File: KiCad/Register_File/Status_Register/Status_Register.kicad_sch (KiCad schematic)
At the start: 43 parts, among them J1 Conn_01x02_Pin, J10 Conn_01x02_Pin, J11 Conn_01x04_Pin, J2 Conn_01x02_Pin, J3 Conn_01x02_Pin, J5 Conn_01x08_Pin, J6 Conn_01x04_Pin, J7 Conn_01x04_Pin, SW2 SW_SPDT, U1 74LS173, U2 74LS173, U3 74LS245, U4 74LS157, U5 74LS157, U6 74LS08, U7 74LS04, U8 74LS245

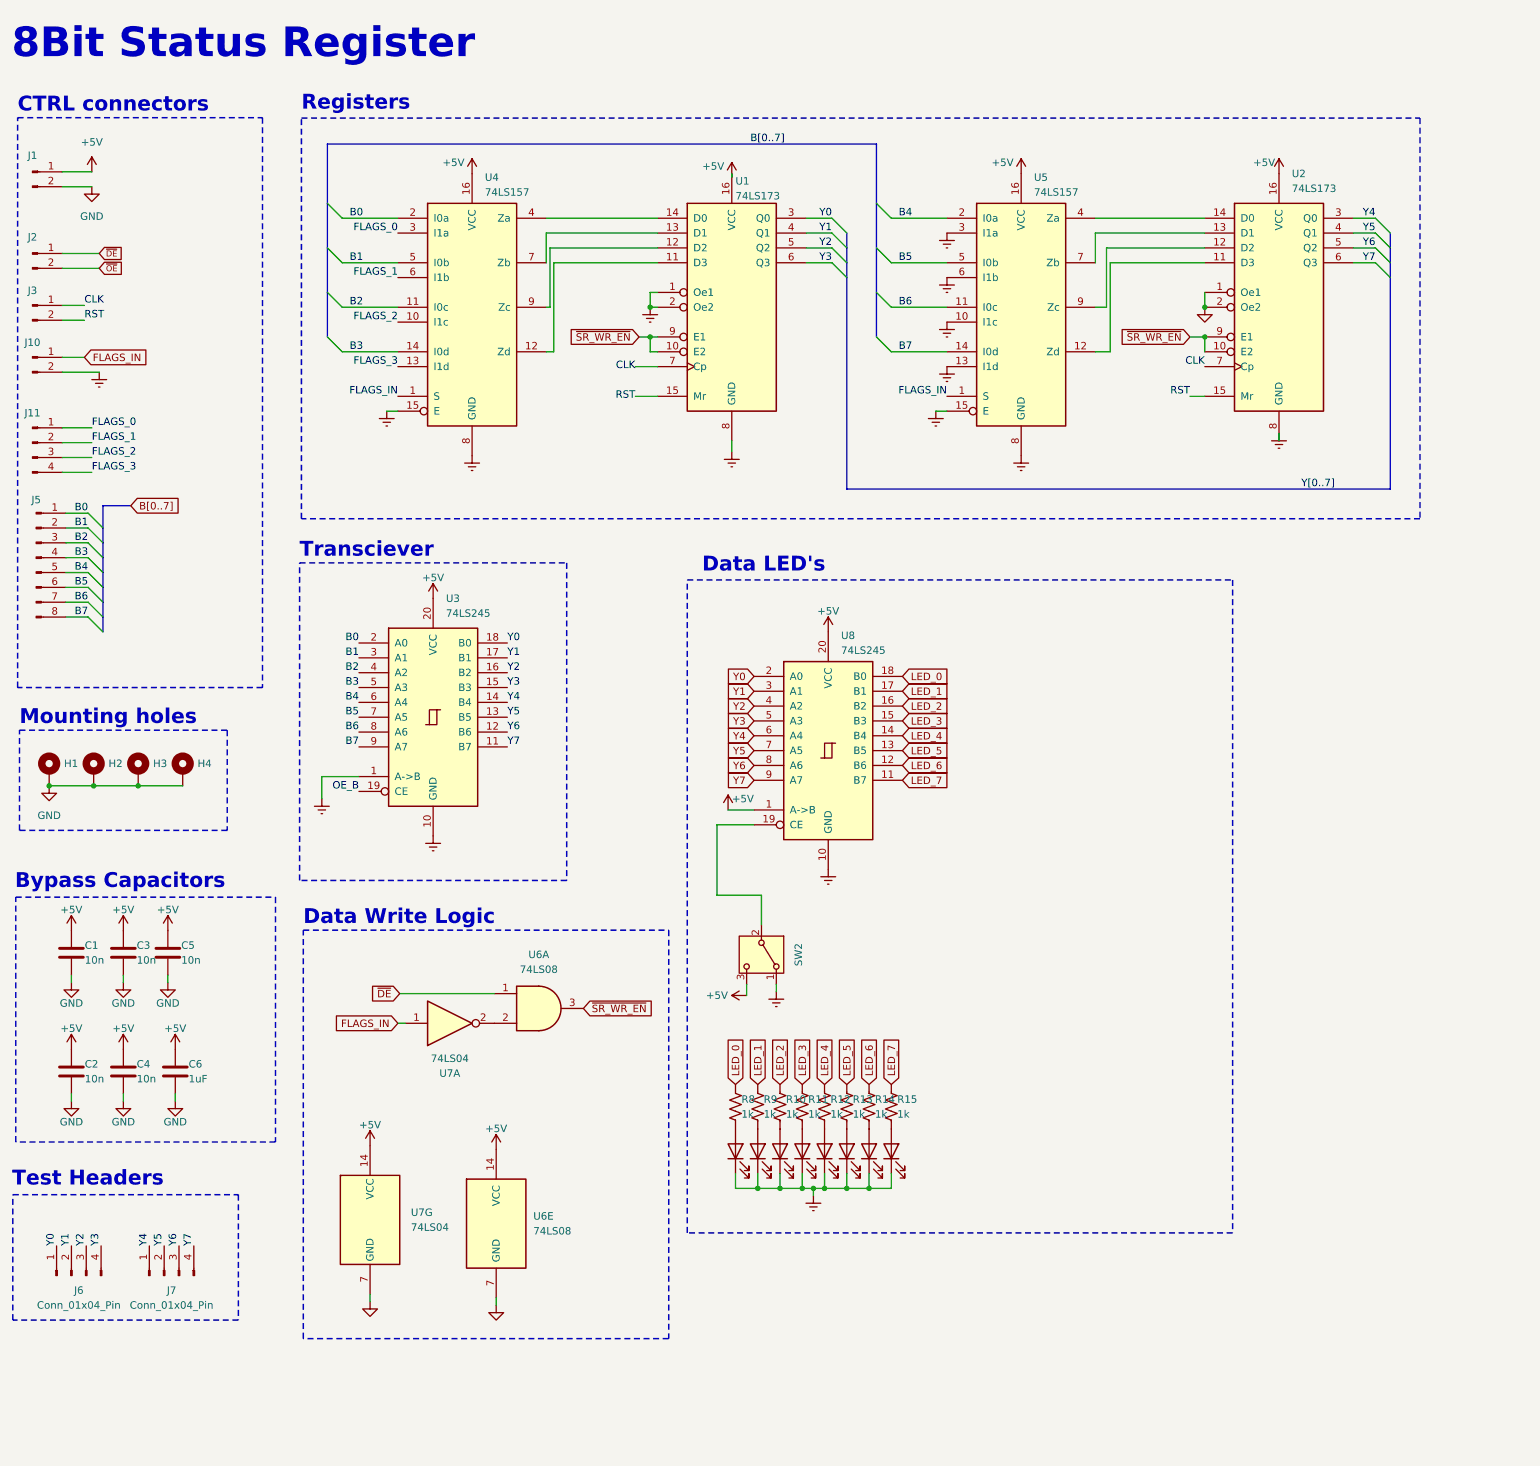
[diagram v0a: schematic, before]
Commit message: created standarts for PCB's
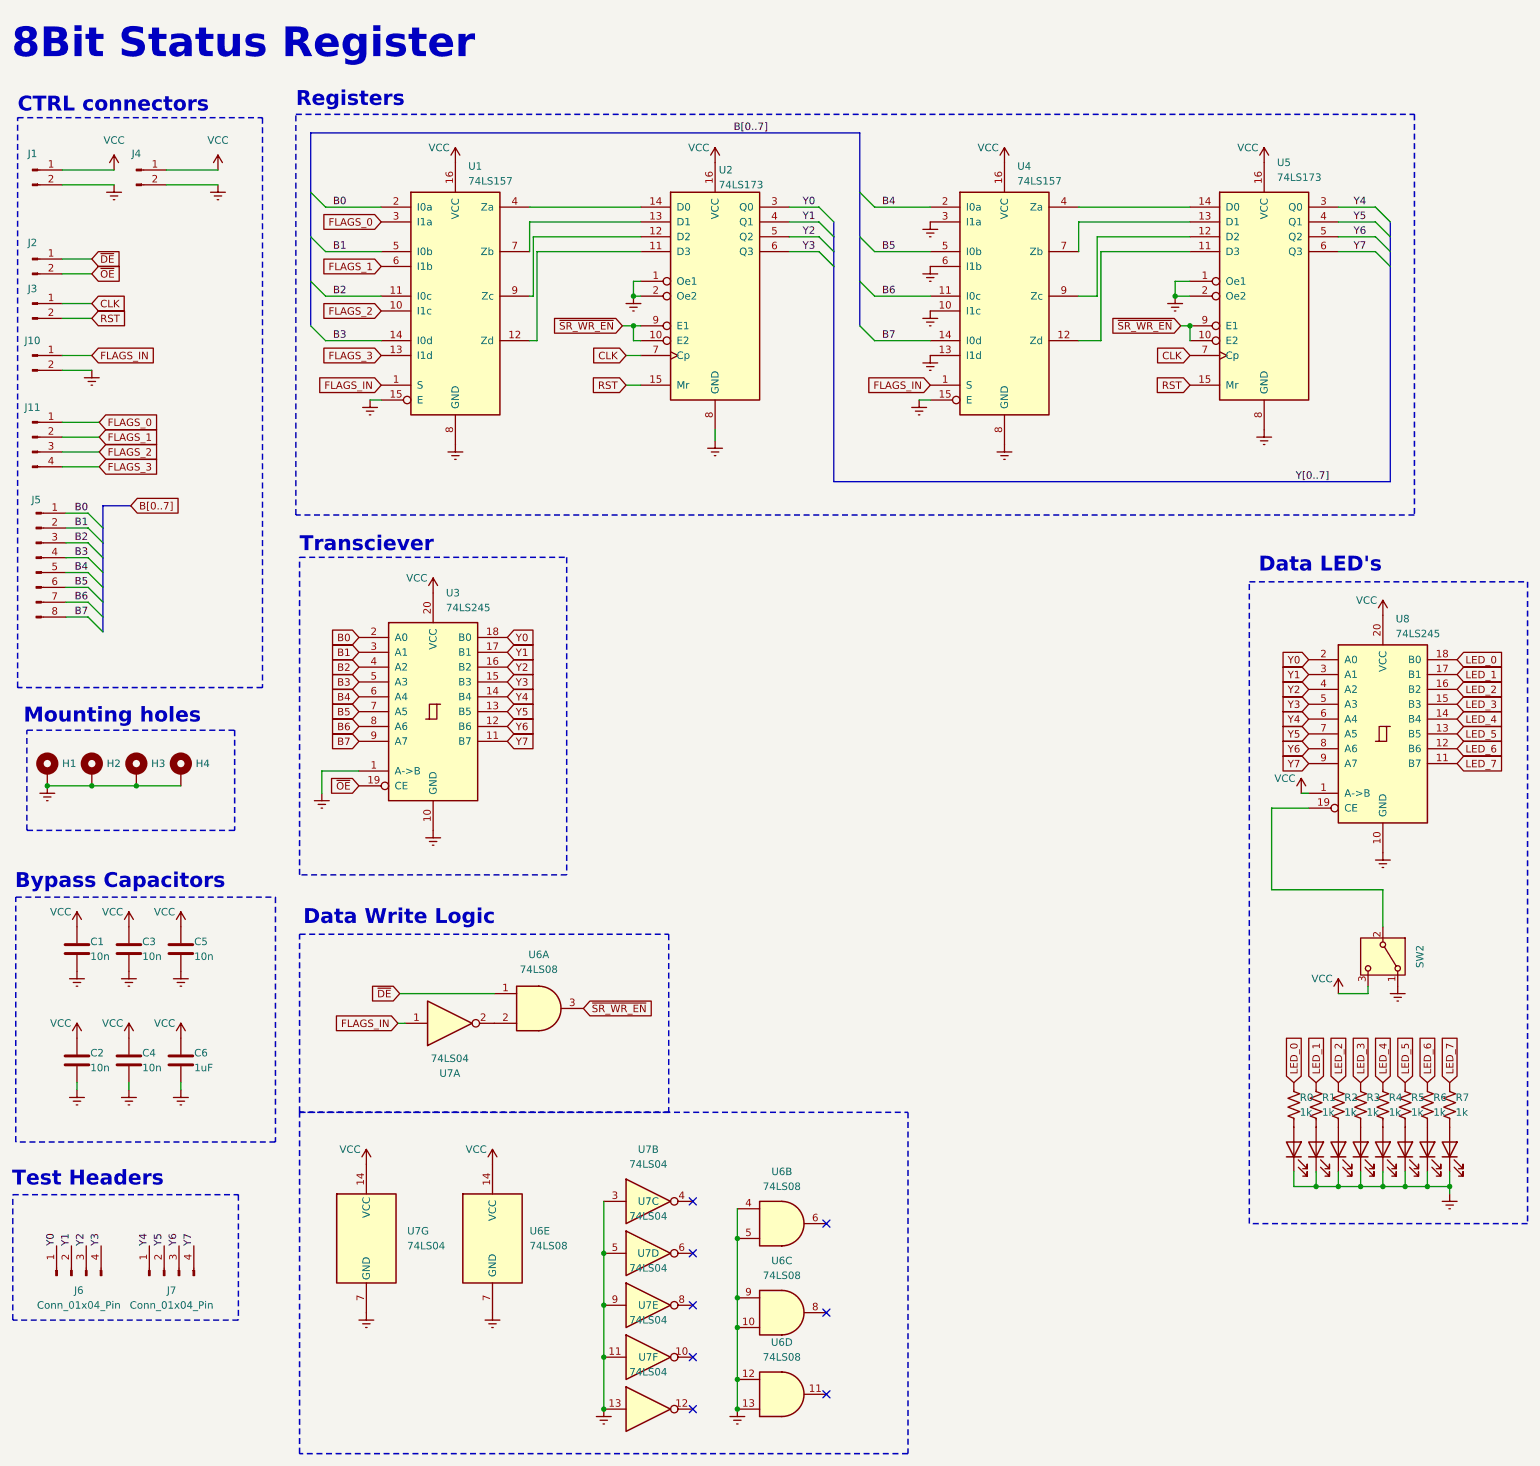
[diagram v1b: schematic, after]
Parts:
- removed D10, D11, D12, D13, D14, D15, D16, D9: LED, LED_THT:LED_Rectangular_W3.0mm_H2.0mm, symbol Device:LED
- removed R10, R11, R12, R13, R14, R15, R8, R9: 1k, Resistor_SMD:R_1206_3216Metric_Pad1.30x1.75mm_HandSolder, symbol Device:R_US
- removed U1: 74LS173, Package_DIP:DIP-16_W7.62mm_Socket_LongPads, symbol 74xx:74LS173
- removed U5: 74LS157, Package_DIP:DIP-16_W7.62mm_Socket_LongPads, symbol 74xx:74LS157
- added D0, D1, D2, D3, D4, D5, D6, D7: LED, LED_THT:LED_Rectangular_W3.0mm_H2.0mm, symbol Device:LED
- added J4: Conn_01x02_Pin, Connector_JST:JST_XH_S2B-XH-A-1_1x02_P2.50mm_Horizontal, symbol Connector:Conn_01x02_Pin
- added R0, R1, R2, R3, R4, R5, R6, R7: 1k, Resistor_SMD:R_1206_3216Metric_Pad1.30x1.75mm_HandSolder, symbol Device:R_US
- added U1: 74LS157, Package_DIP:DIP-16_W7.62mm_Socket_LongPads, symbol 74xx:74LS157
- added U5: 74LS173, Package_DIP:DIP-16_W7.62mm_Socket_LongPads, symbol 74xx:74LS173
- added unit 3 of U6
- added unit 2 of U6
- added unit 4 of U6
- added unit 2 of U7
- added unit 5 of U7
- added unit 6 of U7
- added unit 3 of U7
- added unit 4 of U7
- C1, C2, C3, C4, C5: footprint Capacitor_THT:C_Disc_D3.8mm_W2.6mm_P2.50mm -> Capacitor_SMD:C_1206_3216Metric_Pad1.33x1.80mm_HandSolder
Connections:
- net OE_B is gone; now on net ~{OE}: U3.19 (CE)
- net B0: now also U1.2 (I0a); no longer U4.2 (I0a)
- net B1: now also U1.5 (I0b); no longer U4.5 (I0b)
- net B2: now also U1.11 (I0c); no longer U4.11 (I0c)
- net B3: now also U1.14 (I0d); no longer U4.14 (I0d)
- net B4: now also U4.2 (I0a)
- net B5: now also U4.5 (I0b)
- net B6: now also U4.11 (I0c)
- net B7: now also U4.14 (I0d)
- net CLK: now also U5.7 (Cp)
- net FLAGS_0: now also U1.3 (I1a); no longer U4.3 (I1a)
- net FLAGS_1: now also U1.6 (I1b); no longer U4.6 (I1b)
- net FLAGS_2: now also U1.10 (I1c); no longer U4.10 (I1c)
- net FLAGS_3: now also U1.13 (I1d); no longer U4.13 (I1d)
- net FLAGS_IN: now also U1.1 (S)
- net GND: now also U4.10 (I1c), U4.13 (I1d), U4.3 (I1a), U4.6 (I1b), D0.1 (K), D1.1 (K), D2.1 (K), D3.1 (K), D4.1 (K), D5.1 (K), D6.1 (K), D7.1 (K), J4.2 (Pin_2), U1.15 (E), U1.8 (GND), U5.1 (Oe1), U5.2 (Oe2), U5.8 (GND), U6.10, U6.12, U6.13, U6.4, U6.5, U6.9, U7.11, U7.13, U7.3, U7.5, U7.9
- net LED_0: now also R0.1
- net LED_1: now also R1.1
- net LED_2: now also R2.1
- net LED_3: now also R3.1
- net LED_4: now also R4.1
- net LED_5: now also R5.1
- net LED_6: now also R6.1
- net LED_7: now also R7.1
- net RST: now also U5.15 (Mr)
- net Y0: now also U2.3 (Q0)
- net Y1: now also U2.4 (Q1)
- net Y2: now also U2.5 (Q2)
- net Y3: now also U2.6 (Q3)
- net Y4: now also U5.3 (Q0); no longer U2.3 (Q0)
- net Y5: now also U5.4 (Q1); no longer U2.4 (Q1)
- net Y6: now also U5.5 (Q2); no longer U2.5 (Q2)
- net Y7: now also U5.6 (Q3); no longer U2.6 (Q3)
- net ~{SR_WR_EN}: now also U5.10 (E2), U5.9 (E1)
- net at U4.12 (Zd): now also U5.11 (D3)
- net at U4.4 (Za): now also U5.14 (D0)
- net at U4.7 (Zb): now also U5.13 (D1)
- net at U4.9 (Zc): now also U5.12 (D2)
- net at U2.11 (D3): now also U1.12 (Zd)
- net at U2.12 (D2): now also U1.9 (Zc)
- net at U2.13 (D1): now also U1.7 (Zb)
- net at U2.14 (D0): now also U1.4 (Za)
- net +5V renamed VCC
- net VCC: now also J4.1 (Pin_1), U1.16 (VCC), U5.16 (VCC)
- new net: D1.2 (A), R1.2
- new net: D2.2 (A), R2.2
- new net: D3.2 (A), R3.2
- new net: D5.2 (A), R5.2
- new net: D0.2 (A), R0.2
- new net: D4.2 (A), R4.2
- new net: D7.2 (A), R7.2
- new net: D6.2 (A), R6.2
- no-connect marks 0 -> 8
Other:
- moved on the sheet: C1, C2, C3, C4, C5, C6, J11, J2, SW2, U3, U6E, U7G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
